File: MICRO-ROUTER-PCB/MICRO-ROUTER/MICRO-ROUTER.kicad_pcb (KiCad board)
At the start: 2 copper layers, 85 x 54 mm, 71 parts, among them J2 USB_A, J3 USB_C_Receptacle_USB2.0_16P, J4 Battery Connector, J5 SPI Header, J6 GPIO Header, J7 RJ45 5-2301996-6, Q1 FS8205A, SW2 8Devices Reset, SW3 UART Reset, U1 TP4056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

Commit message: -worked on more layout
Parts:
- moved C2 136.3 mm to (128.8, 160.5)
- moved C1 125.1 mm to (147.2, 150.0)
- moved C3 118.3 mm to (128.2, 137.5)
- moved R7 102.2 mm to (151.2, 153.5)
- moved R3 92.6 mm to (157.8, 165.5)
- moved R2 88.7 mm to (128.2, 139.5)
- moved D6 82.2 mm to (111.0, 125.0)
- moved R11 78.5 mm to (108.3, 114.0)
- moved C14 45.2 mm to (134.3, 101.0)
- moved R1 42.4 mm to (128.8, 162.5)
- moved R17 41.3 mm to (128.0, 95.5)
- moved C16 35.3 mm to (167.7, 149.5)
- moved R16 33.9 mm to (128.5, 106.0)
- moved C19 28.9 mm to (71.0, 216.0)
- moved C8 13.7 mm to (178.8, 139.0)
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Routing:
- net V-UNREG: track 7.20 -> 0.35 mm

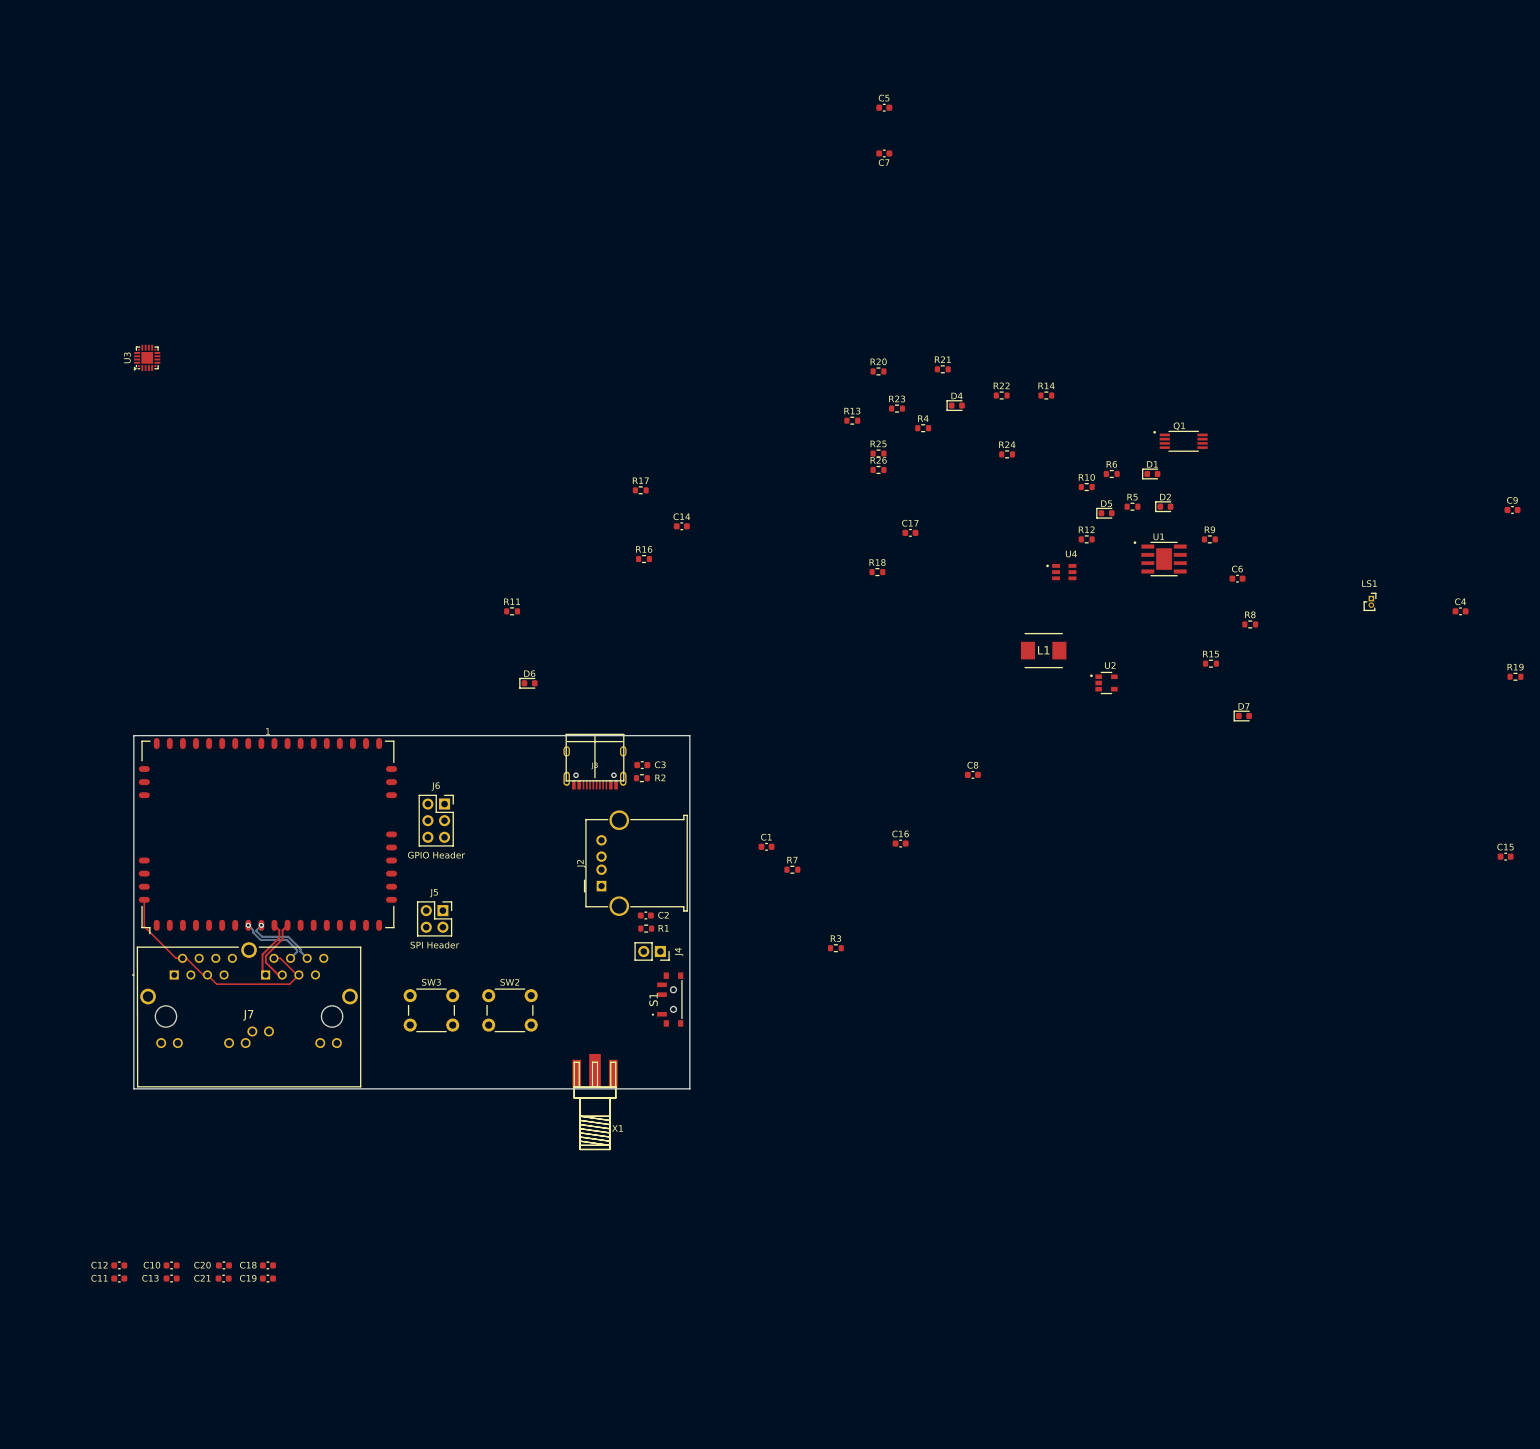
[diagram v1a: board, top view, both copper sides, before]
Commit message: - Finished Usb C layout
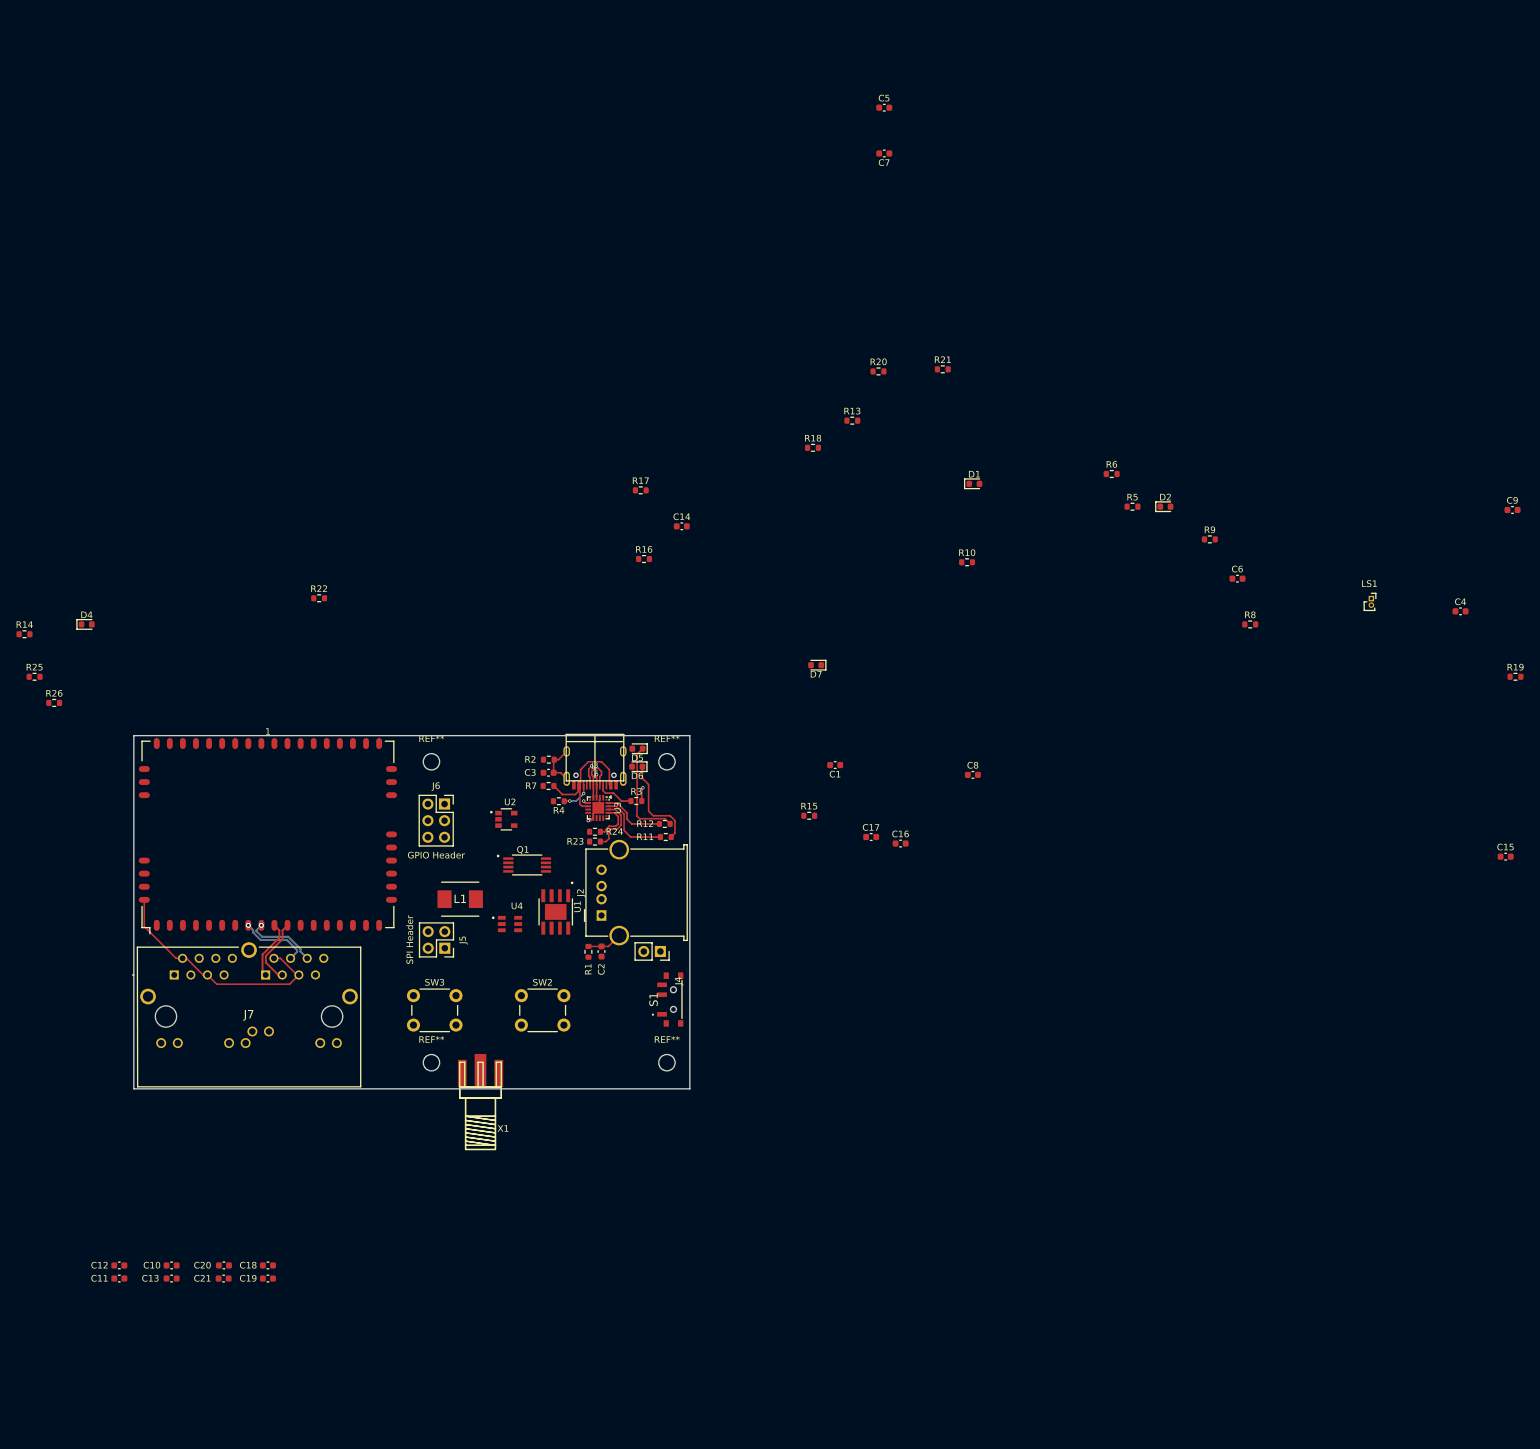
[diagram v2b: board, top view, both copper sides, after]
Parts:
- added REF**: MountingHole_2.5mm, MountingHole:MountingHole_2.5mm, F.Cu at (96.0, 137.0)
- added REF**: MountingHole_2.5mm, MountingHole:MountingHole_2.5mm, F.Cu at (96.0, 183.0)
- added REF**: MountingHole_2.5mm, MountingHole:MountingHole_2.5mm, F.Cu at (132.0, 183.0)
- added REF**: MountingHole_2.5mm, MountingHole:MountingHole_2.5mm, F.Cu at (132.0, 137.0)
- moved R14 160.4 mm to (33.8, 117.5)
- moved D4 137.2 mm to (43.3, 116.0)
- moved R25 133.5 mm to (35.3, 124.0)
- moved R26 131.0 mm to (38.3, 128.0)
- moved Q1 119.5 mm to (110.6, 152.8)
- moved R22 108.9 mm to (78.8, 112.0)
- moved U1 107.5 mm to (115.0, 160.0), turned to -90 degrees
- moved U4 100.4 mm to (108.0, 161.8)
- moved U3 97.4 mm to (121.5, 144.1), turned to -90 degrees
- moved L1 97.0 mm to (100.4, 158.0)
- moved U2 94.1 mm to (107.5, 145.8)
- moved R24 85.4 mm to (121.0, 147.7), turned to 180 degrees
- moved R23 80.7 mm to (121.0, 149.2), turned to 180 degrees
- moved D5 80.2 mm to (127.5, 135.0), turned to 180 degrees
- moved R4 79.7 mm to (115.5, 143.0), turned to 180 degrees
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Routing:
- net VBUS: track 0.00 -> 20.1 mm
- net Net-(D5-K): track 0.00 -> 16.3 mm
- net Net-(D6-K): track 0.00 -> 14.6 mm
- net Net-(U3-~{RXT}/GPIO.3): track 0.00 -> 11.4 mm
- net Net-(U3-~{TXT}/GPIO.2): track 0.00 -> 9.69 mm
- net Net-(U3-TXD): track 0.00 -> 8.73 mm
- net USB-C-D+: track 0.00 -> 8.35 mm, vias 0 -> 2
- net USB-C-D-: track 0.00 -> 8.13 mm
- net Net-(J3-SHIELD): track 0.00 -> 6.85 mm
- net GND: track 0.00 -> 6.55 mm, vias 0 -> 2
- net Net-(U3-RXD): track 0.00 -> 6.17 mm
- net Net-(J3-CC1): track 0.00 -> 5.81 mm
- net Net-(J2-Shield): track 0.00 -> 5.40 mm
- net Net-(J3-CC2): track 0.00 -> 4.95 mm, vias 0 -> 2
- net +3.3V: track 0.00 -> 0.80 mm, vias 0 -> 1

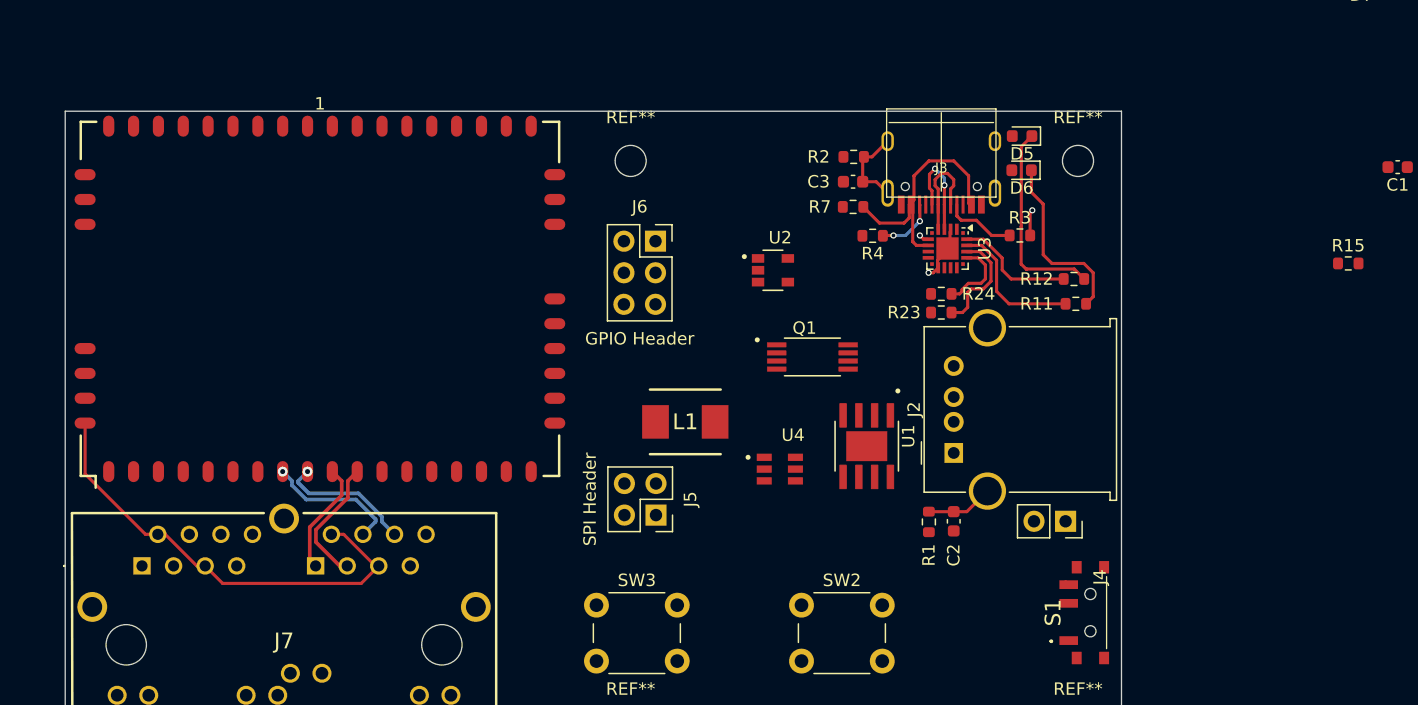
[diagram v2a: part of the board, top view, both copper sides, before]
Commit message: routed rj45 lines
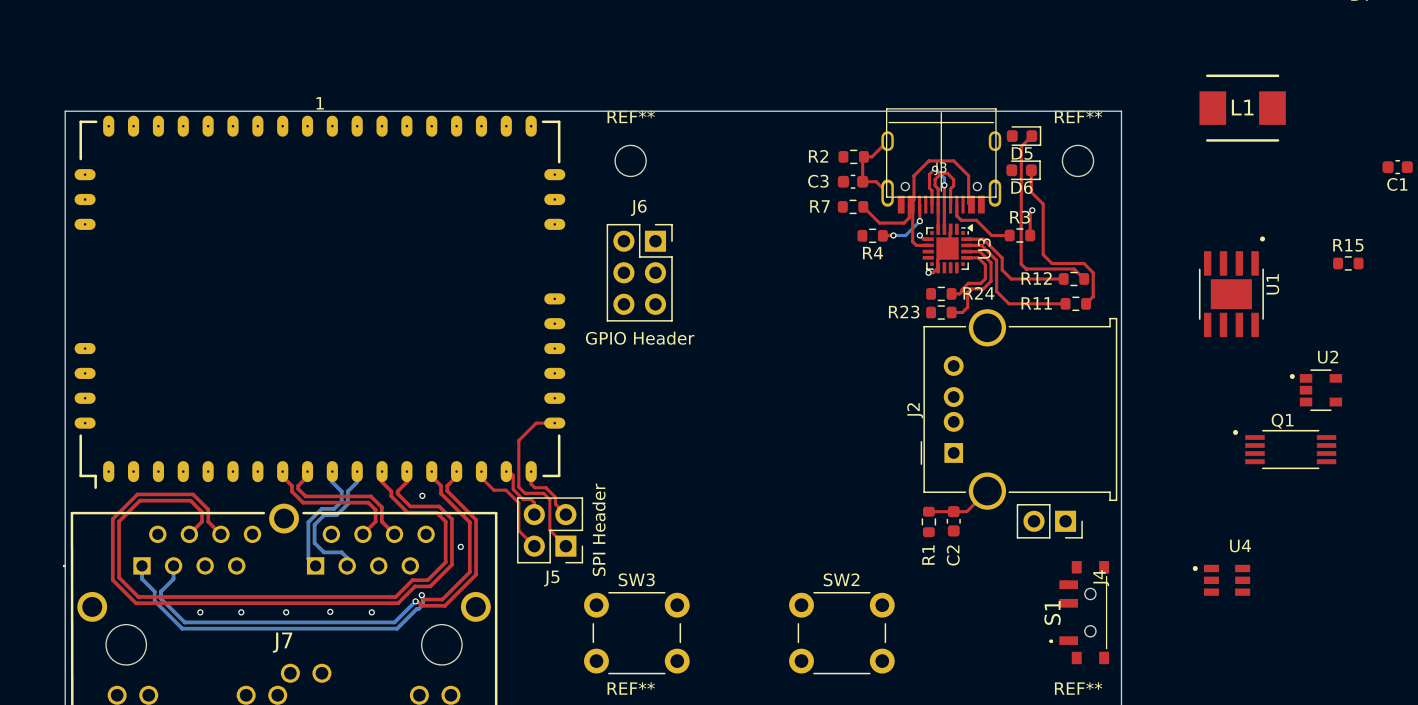
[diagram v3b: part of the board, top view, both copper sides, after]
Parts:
- moved L1 51.5 mm to (145.2, 132.8)
- moved U2 45.1 mm to (151.6, 155.4)
- moved Q1 39.2 mm to (149.1, 160.2)
- moved U4 37.1 mm to (144.0, 170.8)
- moved U1 31.8 mm to (144.3, 147.7)
- moved J5 7.67 mm to (90.8, 168.0)
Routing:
- net ETH0-RX-: track 0.00 -> 56.7 mm
- net ETH0-RX+: track 0.00 -> 53.3 mm
- net ETH0-TX+: track 0.00 -> 42.0 mm, vias 0 -> 1
- net ETH0-TX-: track 0.00 -> 40.7 mm, vias 0 -> 1
- net +2v: track 36.8 -> 0.00 mm
- net SPI 1: track 0.00 -> 14.4 mm
- net SPI 4: track 0.00 -> 8.33 mm
- net SPI 2: track 0.00 -> 6.13 mm
- net SPI 3: track 0.00 -> 4.92 mm
- net ETH1-TX-: track 10.4 -> 11.5 mm
- net ETH1-RX-: track 10.9 -> 11.6 mm, vias 1 -> 0
- net ETH1-RX+: track 10.9 -> 11.6 mm, vias 1 -> 0
- net ETH1-TX+: track 9.16 -> 9.84 mm
- net (no net): vias 0 -> 7

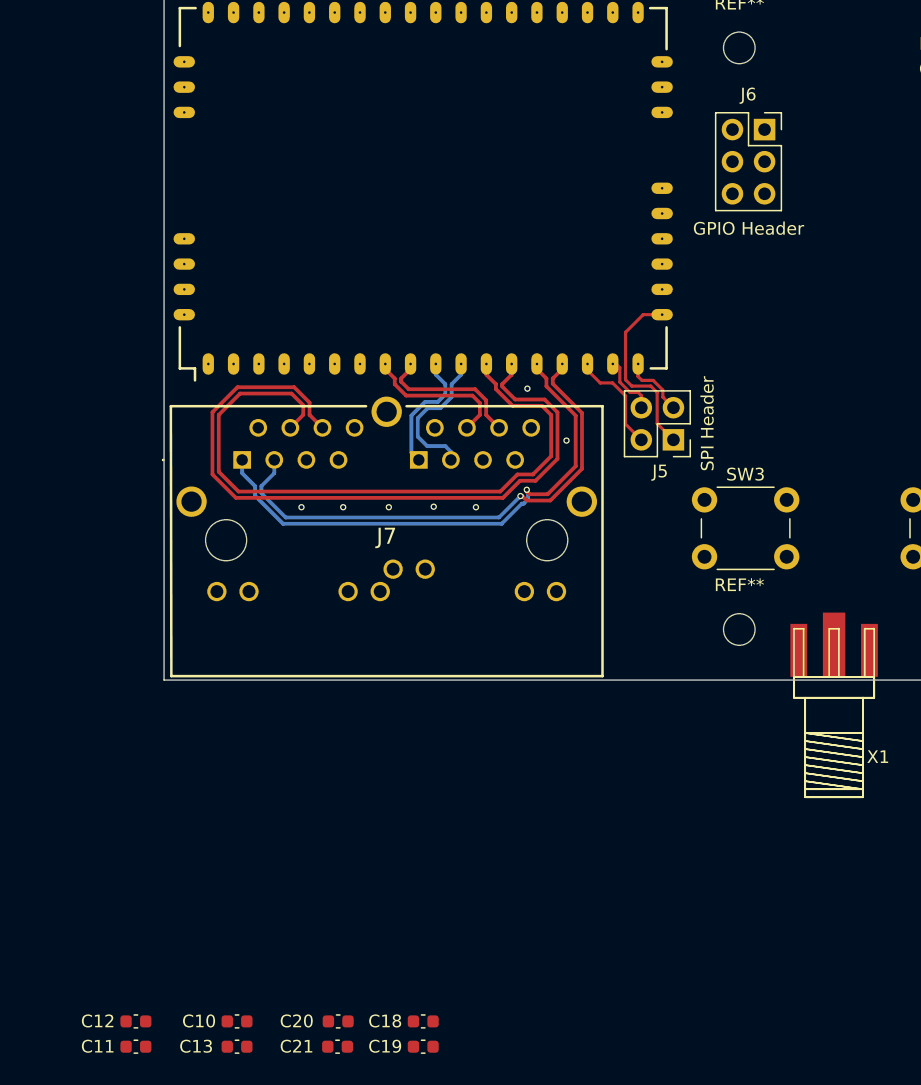
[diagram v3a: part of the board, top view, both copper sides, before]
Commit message: -wired sma connector
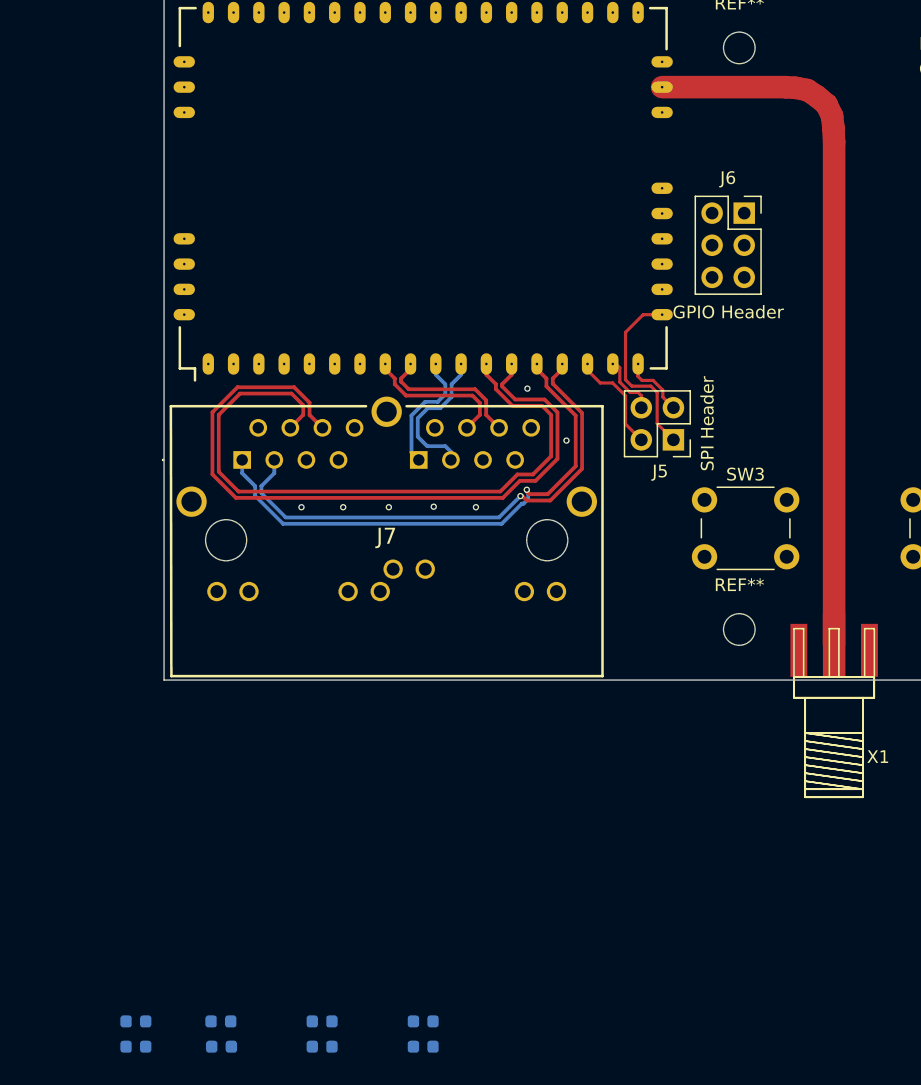
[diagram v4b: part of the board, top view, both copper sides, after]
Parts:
- C10, C11, C12, C13, C18, C19, C20, C21: moved to B.Cu
- moved C11 22.7 mm to (71.0, 216.0), turned to 180 degrees
- moved C12 22.7 mm to (71.0, 214.0), turned to 180 degrees
- moved C18 22.7 mm to (48.3, 214.0), turned to 180 degrees
- moved C19 22.7 mm to (48.3, 216.0), turned to 180 degrees
- moved C20 9.28 mm to (55.0, 214.0), turned to 180 degrees
- moved C21 9.17 mm to (55.0, 216.0), turned to 180 degrees
- moved J6 6.80 mm to (96.4, 150.1)
- moved C10 6.73 mm to (63.0, 214.0), turned to 180 degrees
- moved C13 6.73 mm to (63.0, 216.0), turned to 180 degrees
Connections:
- net Net-(1-ANT0) renamed /ANT1
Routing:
- net /ANT1: track 0.00 -> 56.2 mm
